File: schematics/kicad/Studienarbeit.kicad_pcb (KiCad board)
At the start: 2 copper layers, 73 x 73 mm, 84 parts, among them J2 Conn_01x18, J3 Conn_01x18, J4 Conn_01x01_Pin, J5 Conn_01x01_Pin, J6 Conn_01x01_Pin, J7 Conn_01x01_Pin, J9 SJ2-35853B-SMT-TR, U2 PCM5102, U3 MCP6001-OT, U4 MCP6001-OT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

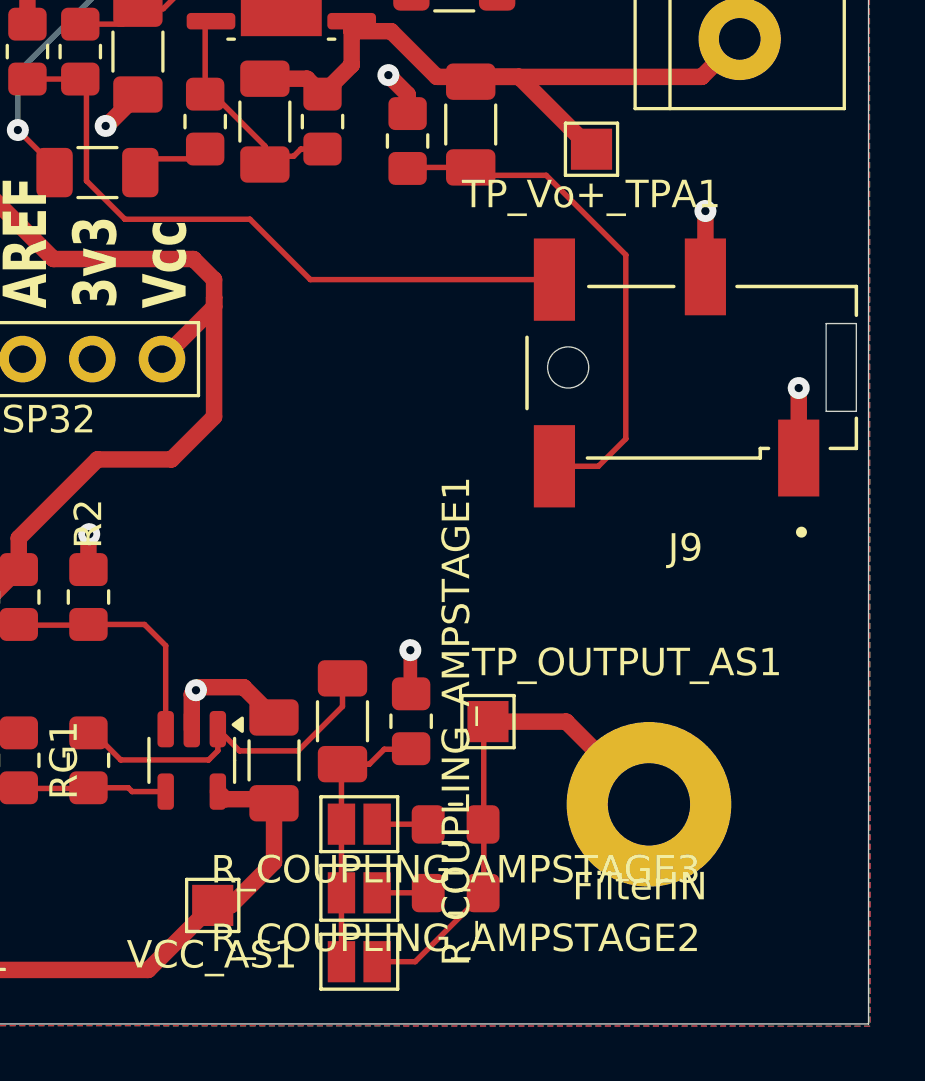
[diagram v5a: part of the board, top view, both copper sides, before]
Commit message: Rezolved Jack footprint issue.
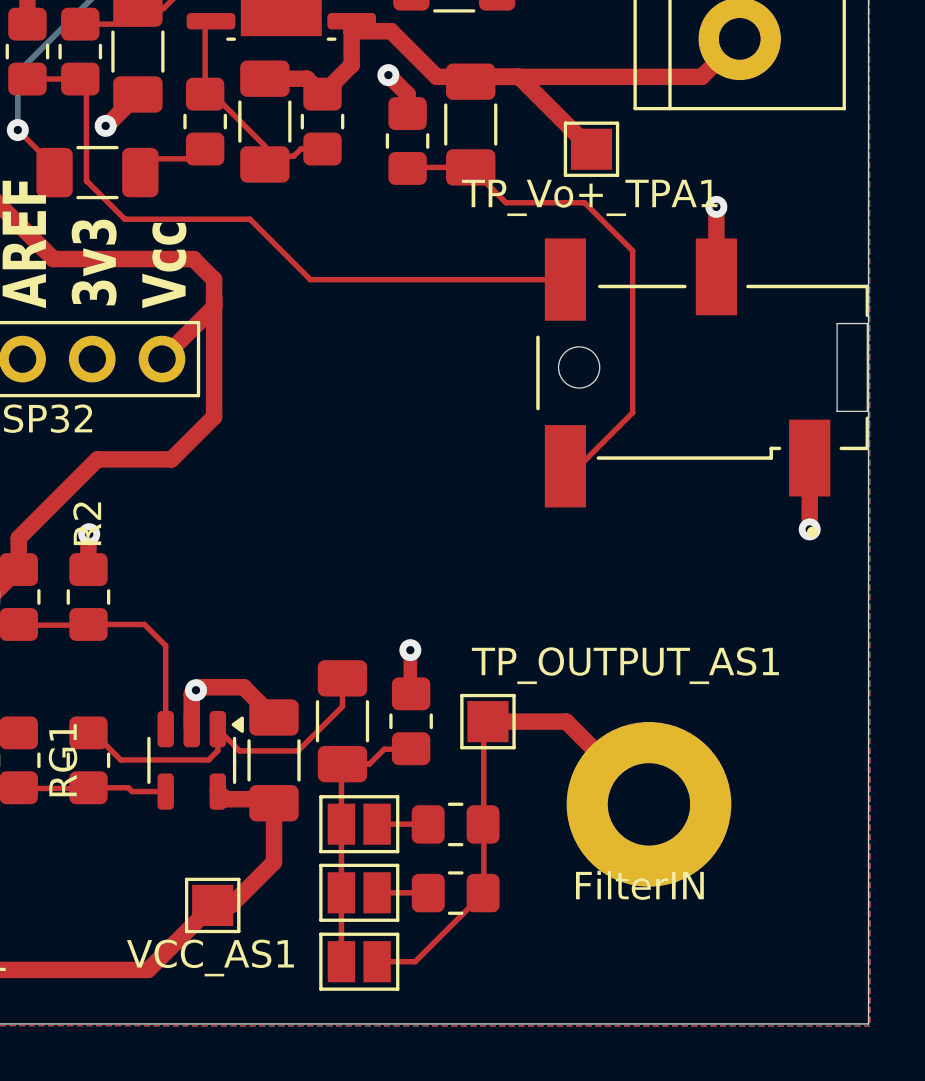
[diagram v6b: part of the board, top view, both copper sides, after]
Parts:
- moved J9 0.40 mm to (274.6, 85.2)
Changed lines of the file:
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@@
 	(footprint "SJ2-35853B-SMT-TR:CUI_SJ2-35853B-SMT-TR"
 		(layer "F.Cu")
-		(at 274.15 85.15 180)
+		(at 274.55 85.15 180)
 		(property "Reference" "J9"
 			(at 0.2243 -6.57451 360)
 			(layer "F.SilkS")
+			(hide yes)
 			(effects
 				(font
@@
 			(at 0 -1.65 -90)
 			(layer "F.SilkS")
+			(hide yes)
 			(effects
 				(font
@@
 			(at 0 -1.65 180)
 			(layer "F.SilkS")
+			(hide yes)
 			(effects
 				(font
@@
 			(at 0 -1.65 180)
 			(layer "F.SilkS")
+			(hide yes)
 			(effects
 				(font
@@
 	)
 	(segment
+		(start 275.05 81.85)
+		(end 275.05 79.3)
+		(width 0.6)
+		(layer "F.Cu")
+		(net 1)
+	)
+	(segment
 		(start 247.9 51.75)
 		(end 245.8 51.75)
@@
 	)
 	(segment
-		(start 274.65 81.85)
-		(end 274.65 79.45)
-		(width 0.6)
-		(layer "F.Cu")
-		(net 1)
-	)
-	(segment
 		(start 236.55 103.05)
 		(end 236.55 101.4375)
@@
 	)
 	(segment
-		(start 278.05 88.45)
-		(end 278.05 85.9)
-		(width 0.6)
-		(layer "F.Cu")
-		(net 1)
-	)
-	(segment
 		(start 226.275 50.7875)
 		(end 228.5625 50.7875)
@@
 	)
 	(segment
+		(start 278.45 88.45)
+		(end 278.45 91.05)
+		(width 0.6)
+		(layer "F.Cu")
+		(net 1)
+	)
+	(segment
 		(start 231.59725 98.34725)
 		(end 231.6 98.35)
@@
 	)
 	(via
+		(at 275.05 79.3)
+		(size 0.8)
+		(drill 0.3)
+		(layers "F.Cu" "B.Cu")
+		(net 1)
+	)
+	(via
 		(at 252.2 91.225)
 		(size 0.8)
@@
 	)
 	(via
-		(at 278.05 85.9)
+		(at 247.1 102.35)
 		(size 0.8)
 		(drill 0.3)
@@
 	)
 	(via
-		(at 247.1 102.35)
+		(at 227.25 38.65)
 		(size 0.8)
 		(drill 0.3)
@@
 	)
 	(via
-		(at 227.25 38.65)
+		(at 278.45 91.05)
 		(size 0.8)
 		(drill 0.3)
@@
 	)
 	(via
-		(at 274.65 79.45)
-		(size 0.8)
-		(drill 0.3)
-		(layers "F.Cu" "B.Cu")
-		(net 1)
-	)
-	(via
 		(at 261.225 48.65)
 		(size 0.8)
@@
 	)
 	(segment
-		(start 270.75 88.75)
-		(end 271.75 87.75)
+		(start 272 80.9)
+		(end 270.25 79.15)
 		(width 0.2)
 		(layer "F.Cu")
@@
 	)
 	(segment
-		(start 266.3875 78.15)
-		(end 266.1 77.8625)
+		(start 270.25 79.15)
+		(end 267.3875 79.15)
 		(width 0.2)
 		(layer "F.Cu")
@@
 	)
 	(segment
-		(start 271.75 81.05)
-		(end 268.85 78.15)
+		(start 269.55 88.75)
+		(end 270.05 88.75)
 		(width 0.2)
 		(layer "F.Cu")
@@
 	)
 	(segment
-		(start 268.85 78.15)
-		(end 266.3875 78.15)
+		(start 272 86.8)
+		(end 272 80.9)
 		(width 0.2)
 		(layer "F.Cu")
@@
 	)
 	(segment
-		(start 271.75 87.75)
-		(end 271.75 81.05)
+		(start 270.05 88.75)
+		(end 272 86.8)
 		(width 0.2)
 		(layer "F.Cu")
@@
 	)
 	(segment
-		(start 263.9 77.9)
-		(end 263.9375 77.8625)
+		(start 267.3875 79.15)
+		(end 266.1 77.8625)
 		(width 0.2)
 		(layer "F.Cu")
@@
 	)
 	(segment
-		(start 269.15 88.75)
-		(end 270.75 88.75)
+		(start 263.9 77.9)
+		(end 263.9375 77.8625)
 		(width 0.2)
 		(layer "F.Cu")
@@
 	)
 	(segment
-		(start 269.15 81.95)
+		(start 269.55 81.95)
 		(end 260.2575 81.95)
 		(width 0.2)
@@
 	)
 	(segment
-		(start 252.1 78.35)
-		(end 252.1 74.8675)
+		(start 260.2575 81.95)
+		(end 258.0575 79.75)
 		(width 0.2)
 		(layer "F.Cu")
@@
 	)
 	(segment
-		(start 249.95 74.6425)
-		(end 251.875 74.6425)
+		(start 258.0575 79.75)
+		(end 253.5 79.75)
 		(width 0.2)
 		(layer "F.Cu")
@@
 	)
 	(segment
-		(start 258.0575 79.75)
-		(end 253.5 79.75)
+		(start 253.5 79.75)
+		(end 252.1 78.35)
 		(width 0.2)
 		(layer "F.Cu")
@@
 	)
 	(segment
-		(start 253.5 79.75)
-		(end 252.1 78.35)
+		(start 252.1 74.8675)
+		(end 251.875 74.6425)
 		(width 0.2)
 		(layer "F.Cu")
@@
 	)
 	(segment
-		(start 260.2575 81.95)
-		(end 258.0575 79.75)
+		(start 252.1 78.35)
+		(end 252.1 74.8675)
 		(width 0.2)
 		(layer "F.Cu")
@@
 	)
 	(segment
-		(start 252.1 74.8675)
+		(start 249.95 74.6425)
 		(end 251.875 74.6425)
 		(width 0.2)
